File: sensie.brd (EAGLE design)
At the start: 38.1 x 25.4 mm, 28 parts, among them J2 BATT, Q1 MOSFET-PCHANNELSMD, Q2 MOSFET-NCHANNELBSS138, Q3 20MHz

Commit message: About to refactor headers.
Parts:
- moved D1 6.94 mm to (35.6, 12.2), turned to 180 degrees
- moved Q1 3.96 mm to (35.7, 18.7), turned to 270 degrees
- moved D2 1.20 mm to (33.4, 14.5), turned to 90 degrees
- renumbered LED2 to PWR
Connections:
- net ANALOG_VPP_ENABLE renamed ANALOG_ENABLE
- removed net N$6: 3.3V.1, 3.3V.2, 3.3V.3, 3.3V.4, 3.3V.5, 3.3V.6, 3.3V.7, Q2.2
- net 3.3V: now also 3.3V.1, 3.3V.2, 3.3V.3, 3.3V.4, 3.3V.5, 3.3V.6, 3.3V.7
- net GND: now also Q2.2
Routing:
- net N$6: track 22.3 -> 0.00 mm
- net 3.3V: track 11.7 -> 29.6 mm
- net VCC_IN: track 36.7 -> 24.1 mm
- net VIN_USB: track 3.36 -> 14.7 mm, vias 0 -> 1
- net N$19: track 1.74 -> 5.53 mm
- net VIN_BATT: track 1.73 -> 3.38 mm
- added copper zone on layer 1, net GND

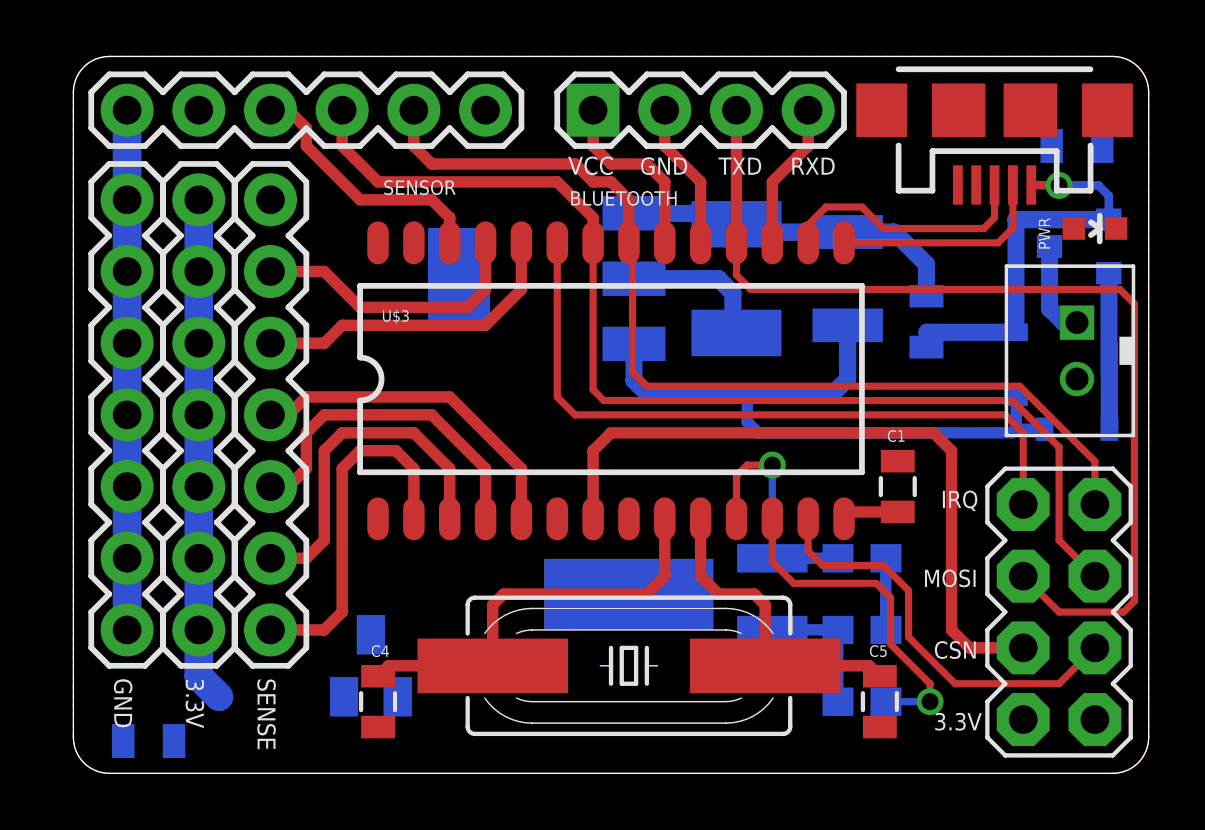
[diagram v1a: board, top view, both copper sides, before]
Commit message: About to refactor uC.
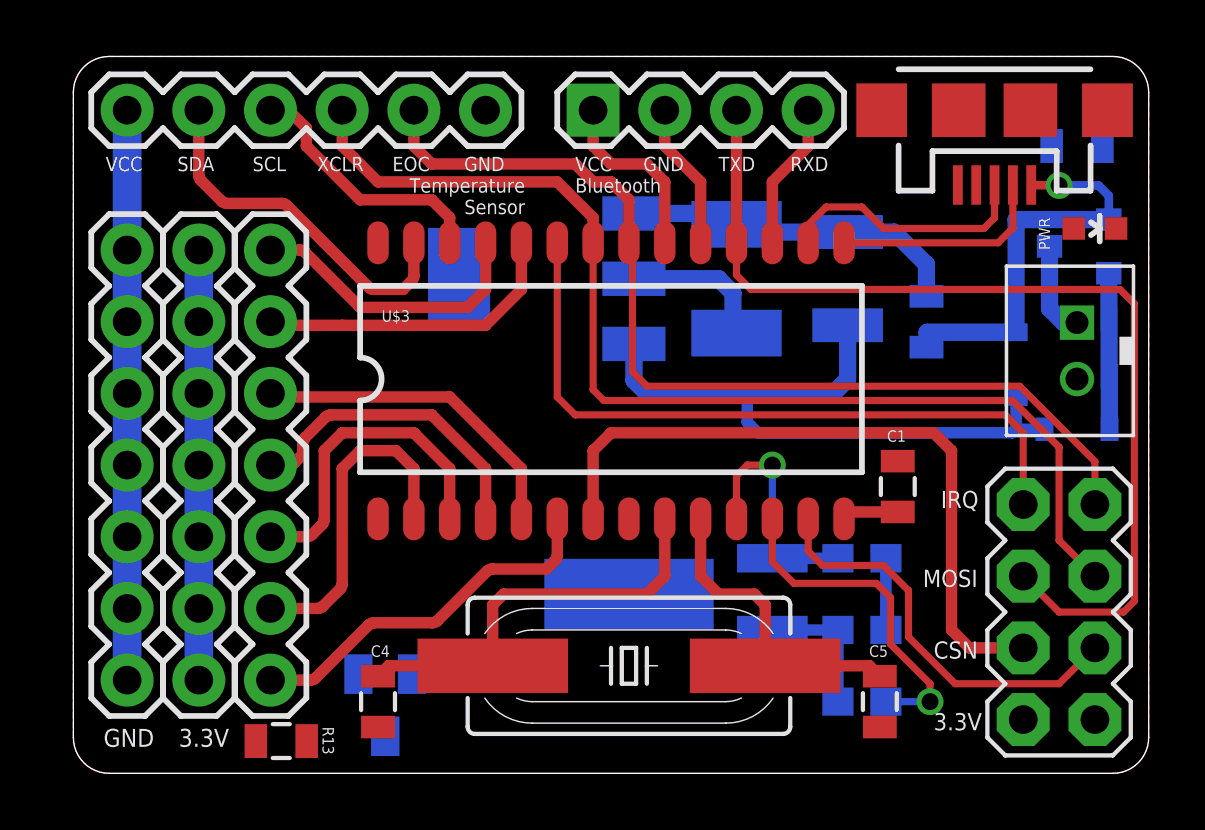
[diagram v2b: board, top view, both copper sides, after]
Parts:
- removed SENSE: (no value), SparkFun-Connectors:1X07
- added JP2: (no value), SparkFun-Connectors:1X07
- moved R13 4.70 mm to (7.37, 1.14), flipped to the top, turned to 0 degrees
- moved 3.3V 1.78 mm to (4.45, 3.30)
- moved GND 1.78 mm to (1.91, 3.30)
- moved Q2 1.49 mm to (11.0, 2.41), turned to 180 degrees
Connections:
- removed net AN6: SENSE.7
- new net COUNTER: JP2.1, U$3.6
- net AN0: now also JP2.2; no longer SENSE.1
- net AN1: now also JP2.3; no longer SENSE.2
- net AN2: now also JP2.4; no longer SENSE.3
- net AN3: now also JP2.5; no longer SENSE.4
- net AN4: now also JP2.6; no longer SENSE.5
- net AN5: now also JP2.7; no longer SENSE.6
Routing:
- net COUNTER: track 0.00 -> 13.3 mm
- net BMP_EOC: track 0.00 -> 13.0 mm
- net 3.3V: track 29.6 -> 26.9 mm
- net GND: track 39.6 -> 41.3 mm
- net AN0: track 12.7 -> 11.9 mm
- net AN2: track 12.0 -> 11.2 mm
- net AN1: track 12.4 -> 11.6 mm
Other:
- board text added: "Bluetooth"
- board text added: "EOC"
- board text added: "SCL"
- board text added: "SDA"
- board text added: "Temperature Sensor"
- board text added: "XCLR"

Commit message: Routing cleanup.
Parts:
- removed PWR: (no value), SparkFun:LED-0603
- removed R3: 330, SparkFun:0805
- moved Q2 13.2 mm to (10.3, 15.6), turned to 0 degrees
- moved R13 7.90 mm to (11.0, 8.13), turned to 270 degrees
- moved U$3 2.03 mm to (21.1, 14.0)
- moved C1 1.78 mm to (31.0, 10.2)
- moved 3.3V 0.38 mm to (4.45, 2.92)
- moved GND 0.38 mm to (1.91, 2.92)
- moved JP2 0.38 mm to (6.99, 2.92)
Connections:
- removed net N$7: PWR.A, R3.2
- net 3.3V: now also SENSOR.1; no longer SENSOR.6
- net GND: now also SENSOR.6, U$2.1; no longer PWR.C, SENSOR.1
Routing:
- net GND: track 41.3 -> 155.0 mm, vias 0 -> 3
- net 3.3V: track 26.9 -> 63.3 mm
- net ANALOG_ENABLE: track 0.00 -> 5.86 mm, vias 0 -> 1
- net AN3: track 11.8 -> 15.9 mm
- net AN2: track 11.2 -> 15.1 mm
- net AN1: track 11.6 -> 15.0 mm
- net COUNTER: track 13.3 -> 16.6 mm
- net AN4: track 11.1 -> 14.2 mm
- net NORDIC_MOSI: track 35.5 -> 32.5 mm
- net T1OSI: track 12.1 -> 9.48 mm
- net AN5: track 10.4 -> 12.9 mm
- net AN0: track 11.9 -> 9.48 mm
- net N$11: track 14.9 -> 17.1 mm
- net NORDIC_CE: track 14.7 -> 12.6 mm
- net BMP_ENABLE: track 9.19 -> 11.3 mm
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- removed copper zone on layer 1, net GND

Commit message: Routing cleanup 2.
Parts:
- moved D1 6.50 mm to (37.0, 18.5), turned to 90 degrees
- moved R5 4.95 mm to (32.1, 20.6)
- moved D2 4.93 mm to (30.6, 18.5)
- moved Q1 1.14 mm to (34.5, 18.7), turned to 180 degrees
- moved R1 0.46 mm to (27.9, 3.00)
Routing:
- net VIN_USB: track 15.0 -> 10.0 mm
- net N$19: track 5.53 -> 1.47 mm
- net VCC_IN: track 24.1 -> 21.4 mm
- net VIN_BATT: track 3.38 -> 2.45 mm

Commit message: Routing cleanup 3.
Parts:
- removed JP1: USB-MICROB, SparkFun-Connectors:USB-MICROB
- added JP3: USB-MICROB, bafoontecha:USB-MICROB
- moved C6 7.37 mm to (16.1, 17.5)
- moved IC1 5.14 mm to (21.8, 16.8), turned to 180 degrees
- moved C3 0.89 mm to (27.9, 6.73)
- moved C7 0.89 mm to (27.9, 4.19)
- moved R1 0.89 mm to (27.9, 2.11)
- moved Y1 0.89 mm to (24.8, 5.46)
- moved C1 0.52 mm to (30.9, 9.65)
- moved U$2 0.52 mm to (35.1, 6.22)
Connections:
- removed net N$3: J2.2
- net GND: now also J2.2, JP3.GND; no longer JP1.GND, JP1.MT1, JP1.MT2
- net N$14: now also JP3.D+; no longer JP1.D+
- net N$15: now also JP3.D-; no longer JP1.D-
- net VIN_USB: now also JP3.VBUS; no longer JP1.VBUS
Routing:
- net 3.3V: track 63.3 -> 94.0 mm
- net GND: track 154.7 -> 134.7 mm
- net VIN_USB: track 10.0 -> 7.29 mm
- net VCC_IN: track 21.4 -> 22.1 mm
- net NORDIC_CSN: track 23.5 -> 22.9 mm

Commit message: Routing cleanup 4.
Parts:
- moved BLUETOOTH 0.89 mm to (18.4, 22.6)
- moved SENSOR 0.89 mm to (1.91, 22.6)
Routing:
- net 3.3V: track 94.0 -> 88.4 mm
- net GND: track 134.7 -> 137.7 mm
- net BMP_EOC: track 15.1 -> 14.2 mm
- net BLUETOOTH_RX: track 5.01 -> 4.13 mm
- net NORDIC_MOSI: track 32.3 -> 31.7 mm

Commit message: About to do ground pours.
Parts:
- removed R13: 10k, SparkFun:0805
- moved Q2 3.68 mm to (10.3, 11.9)
- moved C2 1.60 mm to (25.8, 17.5)
- moved IC1 1.14 mm to (20.7, 16.8)
- moved C6 0.76 mm to (15.4, 17.5)
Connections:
- net 3.3V: now also SENSOR.6; no longer R13.2, SENSOR.1
- net GND: now also SENSOR.1; no longer SENSOR.6
- net VPP: no longer R13.1
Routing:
- net 3.3V: track 88.4 -> 95.4 mm
- net ANALOG_ENABLE: track 5.86 -> 9.49 mm
- net GND: track 137.7 -> 139.7 mm
- net VCC_IN: track 22.1 -> 23.2 mm
- net VPP: track 1.79 -> 2.02 mm, vias 0 -> 1
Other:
- board text added: "MCLR"
- board text added: "PGD"

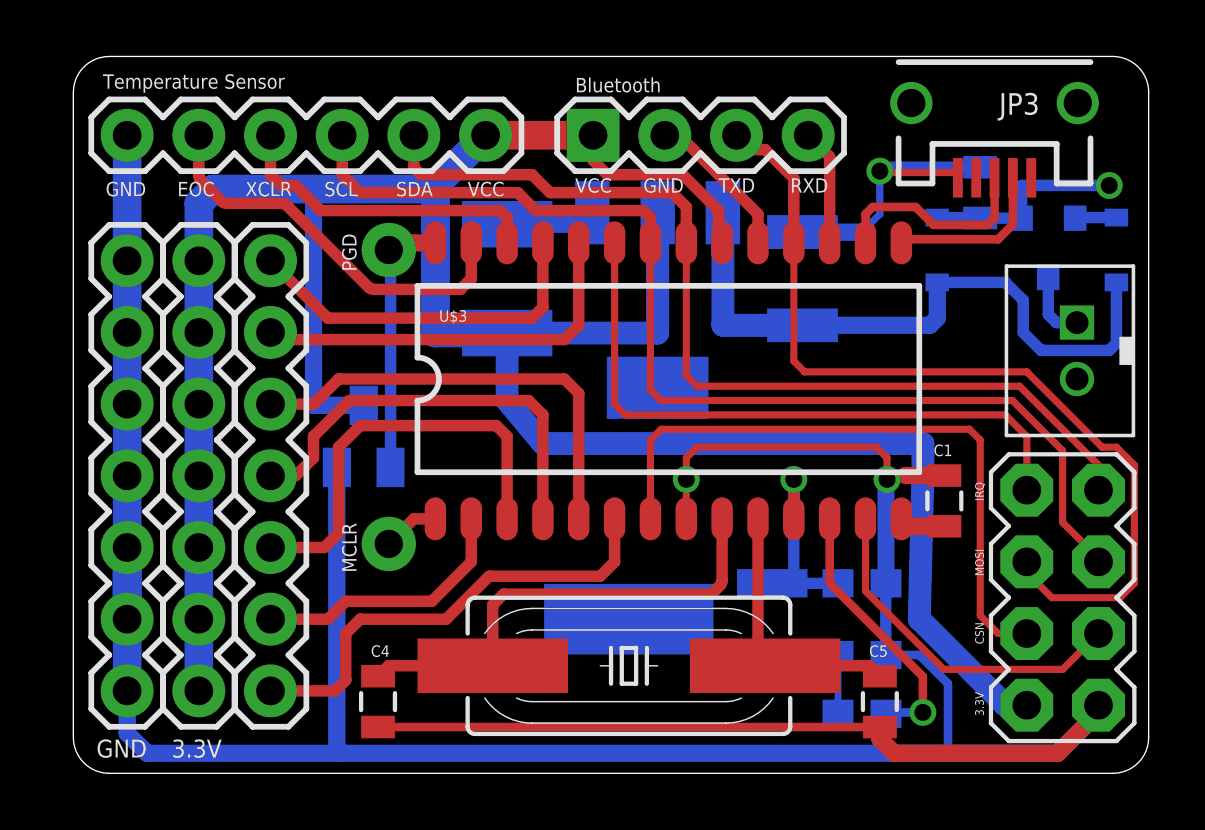
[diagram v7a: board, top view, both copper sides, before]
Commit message: Rerouting Nordic Power.
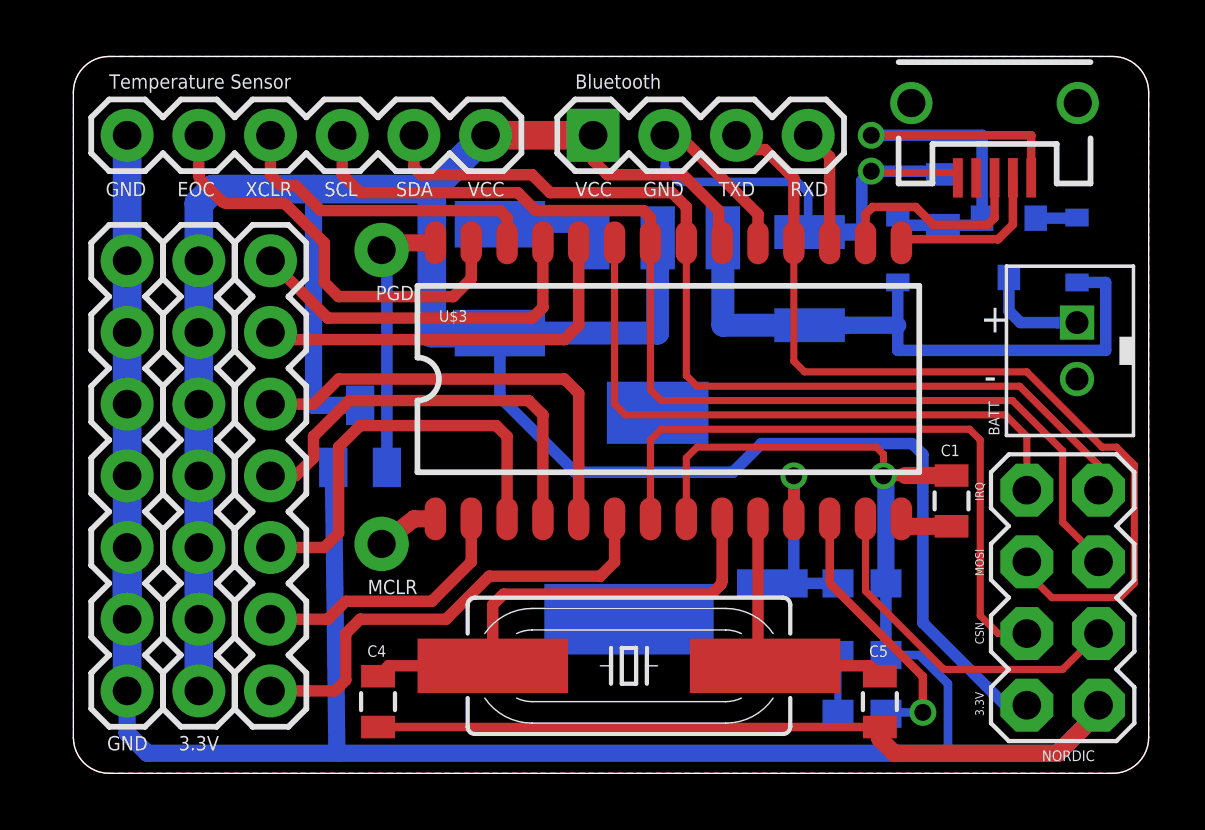
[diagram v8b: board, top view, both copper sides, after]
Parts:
- moved D1 1.40 mm to (35.6, 18.5)
- moved D2 1.40 mm to (29.2, 18.5)
- moved Q1 1.40 mm to (33.1, 18.7)
- moved R5 1.35 mm to (30.8, 20.3)
- moved IC1 0.89 mm to (20.7, 15.9)
- moved C6 0.25 mm to (15.1, 17.5)
- moved C1 0.25 mm to (31.1, 9.65)
- moved C2 0.25 mm to (26.1, 17.5)
- moved Q2 0.13 mm to (10.2, 11.9)
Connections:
- net GND: now also JP3.P$3, JP3.P$4
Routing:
- net VIN_USB: track 7.29 -> 17.7 mm
- net GND: track 139.7 -> 149.5 mm, vias 3 -> 2
- net VIN_BATT: track 2.45 -> 4.50 mm
- net BMP_EOC: track 14.2 -> 15.2 mm
- net VCC_IN: track 23.2 -> 22.5 mm
- added copper zone on layer 1, net GND
- added copper zone on layer 16, net GND
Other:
- board text added: "+"
- board text added: "-"
